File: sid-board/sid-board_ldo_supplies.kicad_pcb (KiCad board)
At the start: 2 copper layers, 39.5 x 40.8 mm, 17 parts, among them J1 ICM_CONN, J2 SID_CONN, J3 5V OUT, J4 3.3V OUT, J5 SPI, U1 SC16IS752IPW, U2 MCP1703A-33, U3 PCA82C250, U4 PCA82C250, U5 MCP1703A-5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

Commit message: Autorouted vs Manual routed. Thinking about adding DIP switch.
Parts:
- U2: value MCP1703A-33 -> MCP1703A-3302_SOT223
- U5: value MCP1703A-5 -> MCP1703A-5002_SOT223

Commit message: Edited some labels
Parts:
- U2: value MCP1703A-3302_SOT223 -> MCP1703A-33
- U5: value MCP1703A-5002_SOT223 -> MCP1703A-5
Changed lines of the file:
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@@
       (effects (font (size 0.5 0.5) (thickness 0.1)))
     )
-    (fp_text value MCP1703A-3302_SOT223 (at 5.334 0.127 180) (layer F.SilkS)
+    (fp_text value MCP1703A-33 (at 5.334 0.127 180) (layer F.SilkS)
       (effects (font (size 0.75 0.75) (thickness 0.16)))
     )
@@
       (effects (font (size 0.5 0.5) (thickness 0.1)))
     )
-    (fp_text value MCP1703A-5002_SOT223 (at 5.334 0) (layer F.SilkS)
+    (fp_text value MCP1703A-5 (at 5.334 0) (layer F.SilkS)
       (effects (font (size 0.75 0.75) (thickness 0.16)))
     )

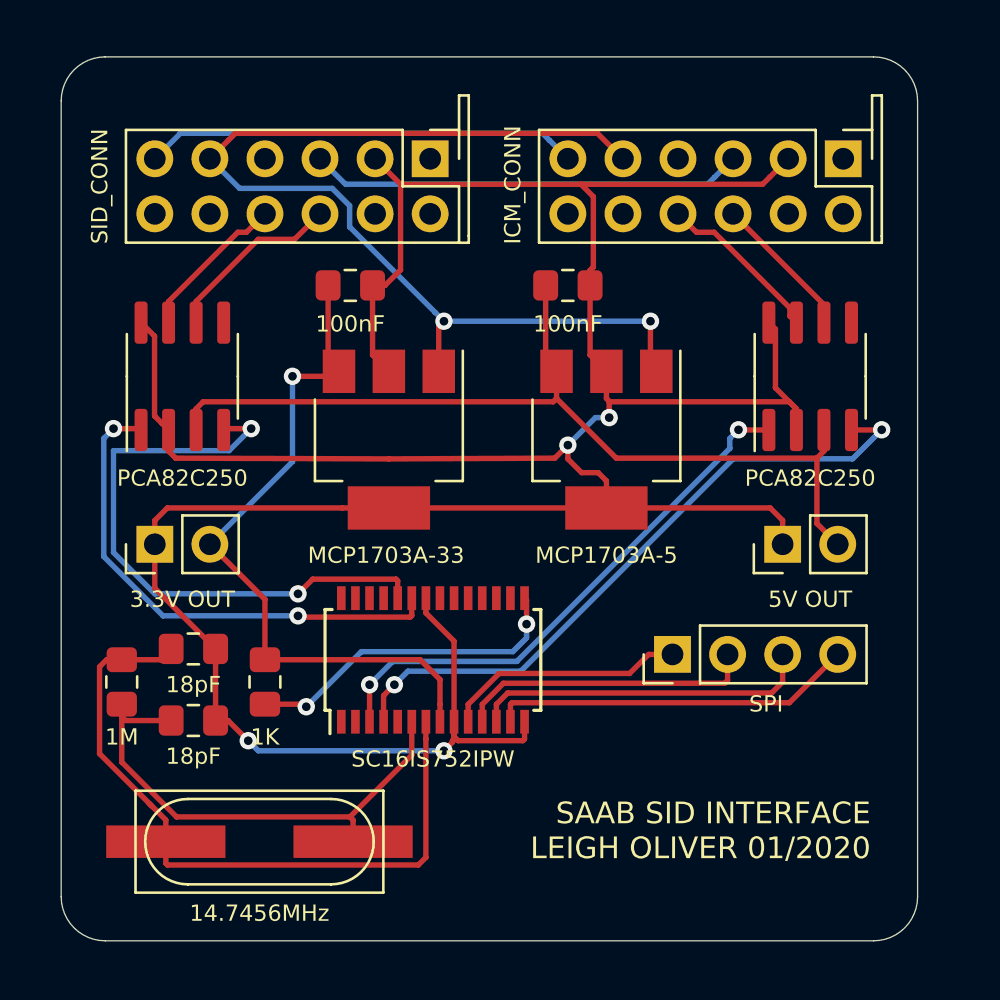
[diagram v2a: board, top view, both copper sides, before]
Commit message: Added bypass DIP switch
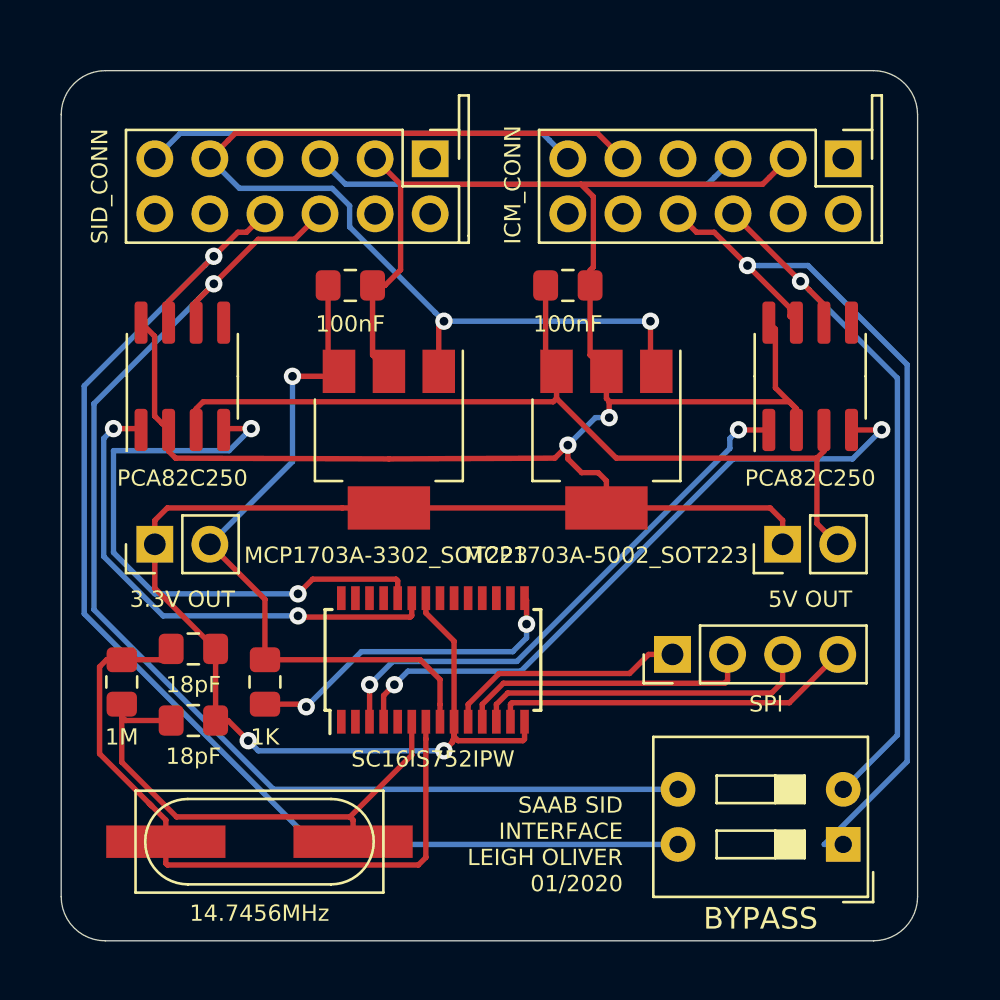
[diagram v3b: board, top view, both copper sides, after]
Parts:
- added BYPASS: SW_DIP_x02, Button_Switch_THT:SW_DIP_SPSTx02_Slide_9.78x7.26mm_W7.62mm_P2.54mm, F.Cu at (100.3, 95.9)
- U2: value MCP1703A-33 -> MCP1703A-3302_SOT223
- U5: value MCP1703A-5 -> MCP1703A-5002_SOT223
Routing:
- net Net-(J2-Pad9): track 7.09 -> 57.8 mm, vias 0 -> 1
- net Net-(J2-Pad10): track 8.36 -> 56.0 mm, vias 0 -> 1
- net Net-(J1-Pad9): track 7.76 -> 41.6 mm, vias 0 -> 1
- net Net-(J1-Pad10): track 6.75 -> 33.1 mm, vias 0 -> 1
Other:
- board size 39.5 x 40.8 mm -> 39.5 x 40.1 mm

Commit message: FINAL BEFORE FABRICATION!
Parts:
- BUS BYPASS: renamed from BYPASS
- J3: value 5V OUT -> GND,5V
- J4: value 3.3V OUT -> GND, 3.3V
- J5: value SPI -> CS,MOSI,MISO,SCLK,INT; footprint Connector_PinHeader_2.54mm:PinHeader_1x04_P2.54mm_Vertical -> Connector_PinHeader_2.54mm:PinHeader_1x05_P2.54mm_Vertical
- U2: value MCP1703A-3302_SOT223 -> MCP1703A-33
- U5: value MCP1703A-5002_SOT223 -> MCP1703A-5
- moved J5 2.54 mm to (89.9, 87.0)
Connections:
- J1 pad 1: Net-(J1-Pad1) -> (no net)
- J1 pad 11: Net-(J1-Pad11) -> (no net)
- J1 pad 12: Net-(J1-Pad12) -> (no net)
- J1 pad 4: Net-(J1-Pad4) -> (no net)
- J1 pad 7: Net-(J1-Pad7) -> (no net)
- J1 pad 8: Net-(J1-Pad8) -> (no net)
- J2 pad 1: Net-(J2-Pad1) -> (no net)
- J2 pad 11: Net-(J2-Pad11) -> (no net)
- J2 pad 12: Net-(J2-Pad12) -> (no net)
- J2 pad 4: Net-(J2-Pad4) -> (no net)
- J2 pad 7: Net-(J2-Pad7) -> (no net)
- J2 pad 8: Net-(J2-Pad8) -> (no net)
- R1 pad 1: Net-(R1-Pad1) -> Net-(J5-Pad5)
- U1 pad 1: Net-(U1-Pad1) -> (no net)
- U1 pad 15: Net-(R1-Pad1) -> Net-(J5-Pad5)
- U1 pad 16: Net-(U1-Pad16) -> (no net)
- U1 pad 17: Net-(U1-Pad17) -> (no net)
- U1 pad 18: Net-(U1-Pad18) -> (no net)
- U1 pad 19: Net-(U1-Pad19) -> (no net)
- U1 pad 2: Net-(U1-Pad2) -> (no net)
- U1 pad 20: Net-(U1-Pad20) -> (no net)
- U1 pad 21: Net-(U1-Pad21) -> (no net)
- U1 pad 25: Net-(U1-Pad25) -> (no net)
- U1 pad 26: Net-(U1-Pad26) -> (no net)
- U1 pad 27: Net-(U1-Pad27) -> (no net)
- U1 pad 28: Net-(U1-Pad28) -> (no net)
- U1 pad 5: Net-(U1-Pad5) -> (no net)
- U3 pad 5: Net-(U3-Pad5) -> (no net)
- U4 pad 5: Net-(U4-Pad5) -> (no net)
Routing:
- net Net-(J5-Pad5): track 0.00 -> 30.2 mm, vias 0 -> 2
- net Net-(R1-Pad1): track 15.3 -> 0.00 mm, vias 2 -> 0
- net Net-(J5-Pad3): track 15.7 -> 12.4 mm
- net Net-(J5-Pad2): track 13.8 -> 10.5 mm
- net Net-(J5-Pad1): track 11.2 -> 8.61 mm
- net Net-(J5-Pad4): track 16.8 -> 14.3 mm

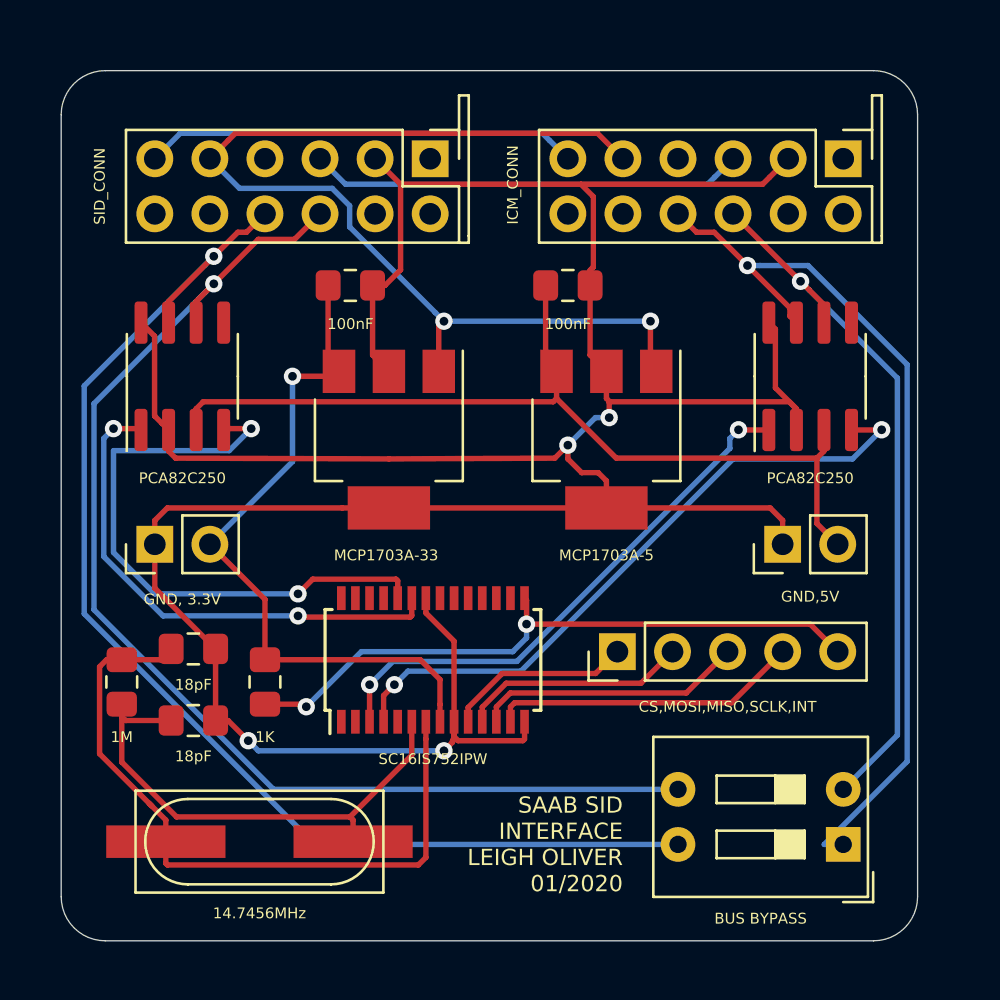
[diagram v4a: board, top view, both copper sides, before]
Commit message: Updated edge cuts
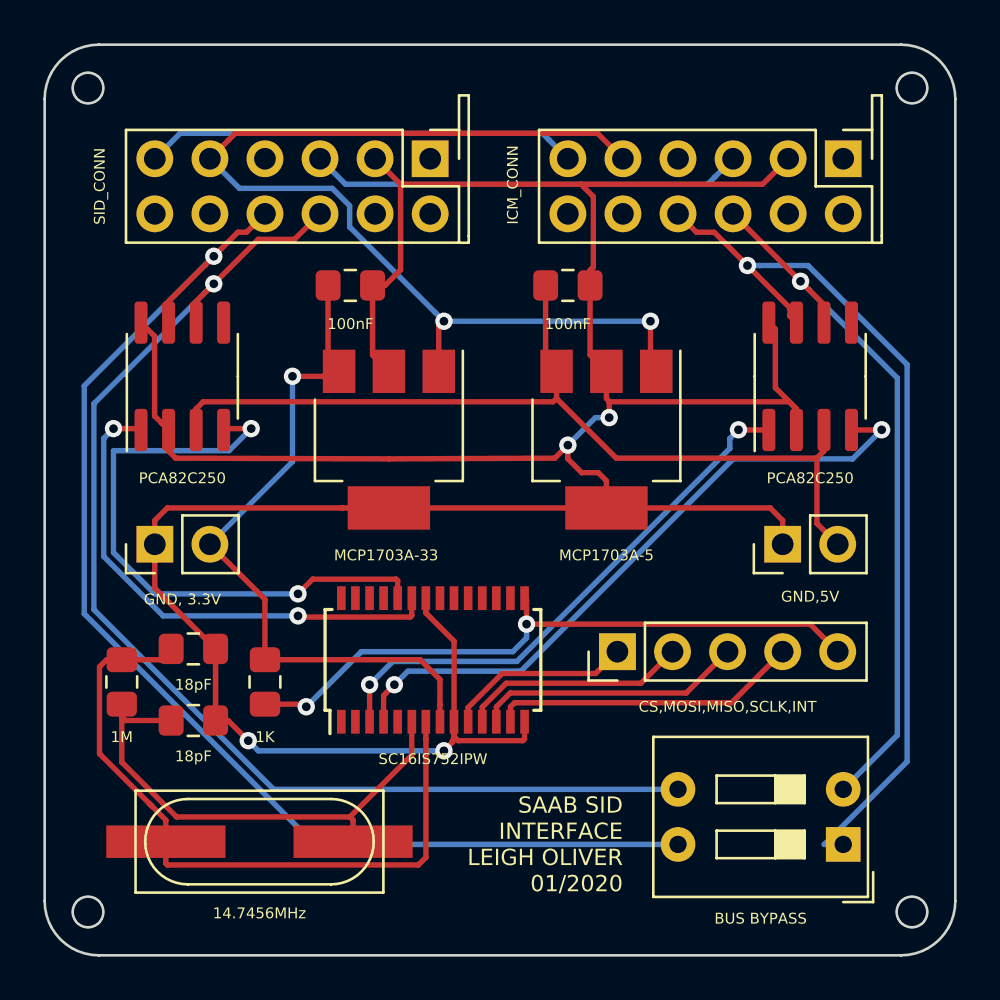
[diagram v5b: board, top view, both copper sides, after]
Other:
- board size 39.5 x 40.1 mm -> 42 x 42 mm
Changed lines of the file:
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@@
   (general
     (thickness 1.6)
-    (drawings 9)
+    (drawings 13)
     (tracks 268)
     (zones 0)
@@
     )
   )
+  (gr_circle (center 103.5 99) (end 104.207107 99) (layer Edge.Cuts) (width 0.12))
+  (gr_circle (center 65.5 99) (end 66.207107 99) (layer Edge.Cuts) (width 0.12))
+  (gr_circle (center 103.5 61) (end 104.207107 61) (layer Edge.Cuts) (width 0.12))
+  (gr_circle (center 65.5 61) (end 66.207107 61) (layer Edge.Cuts) (width 0.12))
+  (gr_arc (start 66 98.5) (end 63.5 98.5) (angle -90) (layer Edge.Cuts) (width 0.12))
+  (gr_arc (start 103 98.5) (end 103 101) (angle -90) (layer Edge.Cuts) (width 0.12))
+  (gr_arc (start 103 61.5) (end 105.5 61.5) (angle -90) (layer Edge.Cuts) (width 0.12))
+  (gr_arc (start 66 61.5) (end 66 59) (angle -90) (layer Edge.Cuts) (width 0.12))
+  (gr_line (start 63.5 98.5) (end 63.5 61.5) (layer Edge.Cuts) (width 0.12))
+  (gr_line (start 103 101) (end 66 101) (layer Edge.Cuts) (width 0.12))
+  (gr_line (start 105.5 61.5) (end 105.5 98.5) (layer Edge.Cuts) (width 0.12))
+  (gr_line (start 66 59) (end 103 59) (layer Edge.Cuts) (width 0.12))
   (gr_text "SAAB SID\nINTERFACE\nLEIGH OLIVER\n01/2020" (at 90.17 95.885) (layer F.SilkS)
     (effects (font (size 0.75 0.75) (thickness 0.1875)) (justify right))
   )
-  (gr_arc (start 101.727 62.23) (end 103.759 62.23) (angle -90) (layer Edge.Cuts) (width 0.05))
-  (gr_arc (start 101.727 98.298) (end 101.727 100.33) (angle -90) (layer Edge.Cuts) (width 0.05))
-  (gr_arc (start 66.294 98.298) (end 64.262 98.298) (angle -90) (layer Edge.Cuts) (width 0.05))
-  (gr_arc (start 66.294 62.23) (end 66.294 60.198) (angle -90) (layer Edge.Cuts) (width 0.05))
-  (gr_line (start 64.262 98.298) (end 64.262 62.23) (layer Edge.Cuts) (width 0.05))
-  (gr_line (start 101.727 100.33) (end 66.294 100.33) (layer Edge.Cuts) (width 0.05))
-  (gr_line (start 103.759 62.23) (end 103.759 98.298) (layer Edge.Cuts) (width 0.05))
-  (gr_line (start 66.294 60.198) (end 101.727 60.198) (layer Edge.Cuts) (width 0.05))
   (segment (start 99.441 70.993) (end 99.441 71.82) (width 0.25) (layer F.Cu) (net 1) (status 30))
   (segment (start 95.25 66.802) (end 98.3615 69.9135) (width 0.25) (layer F.Cu) (net 1) (status 30))
@@
   (segment (start 80.432 91.764) (end 80.432 90.226) (width 0.25) (layer F.Cu) (net 16) (status 20))
   (segment (start 77.581 94.615) (end 80.432 91.764) (width 0.25) (layer F.Cu) (net 16))
-  (via (at 85.725 85.725) (size 0.8) (drill 0.4) (layers F.Cu B.Cu) (net 21))
-  (via (at 75.565 89.535) (size 0.8) (drill 0.4) (layers F.Cu B.Cu) (net 21))
-  (segment (start 75.447 89.417) (end 75.565 89.535) (width 0.25) (layer F.Cu) (net 21))
-  (segment (start 73.66 89.417) (end 75.447 89.417) (width 0.25) (layer F.Cu) (net 21) (status 10))
-  (segment (start 85.725 84.619) (end 85.632 84.526) (width 0.25) (layer F.Cu) (net 21) (status 30))
-  (segment (start 85.725 85.725) (end 85.725 84.619) (width 0.25) (layer F.Cu) (net 21) (status 20))
-  (segment (start 85.725 85.725) (end 85.725 86.36) (width 0.25) (layer B.Cu) (net 21))
-  (segment (start 85.725 86.36) (end 85.09 86.995) (width 0.25) (layer B.Cu) (net 21))
-  (segment (start 78.105 86.995) (end 75.565 89.535) (width 0.25) (layer B.Cu) (net 21))
-  (segment (start 85.09 86.995) (end 78.105 86.995) (width 0.25) (layer B.Cu) (net 21))
   (via (at 75.184 84.328) (size 0.8) (drill 0.4) (layers F.Cu B.Cu) (net 17))
   (via (at 73.025 76.708) (size 0.8) (drill 0.4) (layers F.Cu B.Cu) (net 17))
@@
   (segment (start 78.486 90.222) (end 78.482 90.226) (width 0.25) (layer F.Cu) (net 20) (status 30))
   (segment (start 78.486 88.519) (end 78.486 90.222) (width 0.25) (layer F.Cu) (net 20) (status 20))
+  (via (at 85.725 85.725) (size 0.8) (drill 0.4) (layers F.Cu B.Cu) (net 21))
+  (via (at 75.565 89.535) (size 0.8) (drill 0.4) (layers F.Cu B.Cu) (net 21))
+  (segment (start 75.447 89.417) (end 75.565 89.535) (width 0.25) (layer F.Cu) (net 21))
+  (segment (start 73.66 89.417) (end 75.447 89.417) (width 0.25) (layer F.Cu) (net 21) (status 10))
+  (segment (start 85.725 84.619) (end 85.632 84.526) (width 0.25) (layer F.Cu) (net 21) (status 30))
+  (segment (start 85.725 85.725) (end 85.725 84.619) (width 0.25) (layer F.Cu) (net 21) (status 20))
+  (segment (start 85.725 85.725) (end 85.725 86.36) (width 0.25) (layer B.Cu) (net 21))
+  (segment (start 85.725 86.36) (end 85.09 86.995) (width 0.25) (layer B.Cu) (net 21))
+  (segment (start 78.105 86.995) (end 75.565 89.535) (width 0.25) (layer B.Cu) (net 21))
+  (segment (start 85.09 86.995) (end 78.105 86.995) (width 0.25) (layer B.Cu) (net 21))
   (segment (start 98.806 85.725) (end 100.076 86.995) (width 0.25) (layer F.Cu) (net 21))
   (segment (start 85.725 85.725) (end 98.806 85.725) (width 0.25) (layer F.Cu) (net 21))
